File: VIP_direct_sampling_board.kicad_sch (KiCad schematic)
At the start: 32 parts, among them U1 ${SIM.PARAMS}, U10 LM4132xMF-1.8, U11 DC4759J5020AHF-1, U12 LAT-3, U2 TMUX1104DGSR, U7 MAR-8ASM+, U8 RBP-140+, U9 TSS-23ULN+, X1 B3715

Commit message: PWR progress
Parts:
- added C10: Cbypass, symbol Device:C
- added C8: C, symbol Device:C
- added C9: CBlock, symbol Device:C
- added L4: L, symbol Device:L
- added R10: Rbias, symbol Device:R_US
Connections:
- net GND: now also C10.2; no longer U7.3 (RF-OUT/DC-IN)
- net at U12.2 (OUT): now also C8.1; no longer U7.1 (RF-IN)
- new net: L4.2, R10.2
- new net: C9.1, L4.1, U7.3 (RF-OUT/DC-IN)
- new net: C8.2, U7.1 (RF-IN)
- new net 5V_SW: C10.1, R10.1
- new net RF_OUT: C9.2
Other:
- added sheet power (power.kicad_sch)
- note added: "3.7V"
- note added: "4:1 RF MUX"
- note added: "Bandpass Filter"
- note added: "RFFE First LNA"
- note added: "RFFE Monolithic Amplifier"
- note added: "SAW Filter"
- moved on the sheet: U7

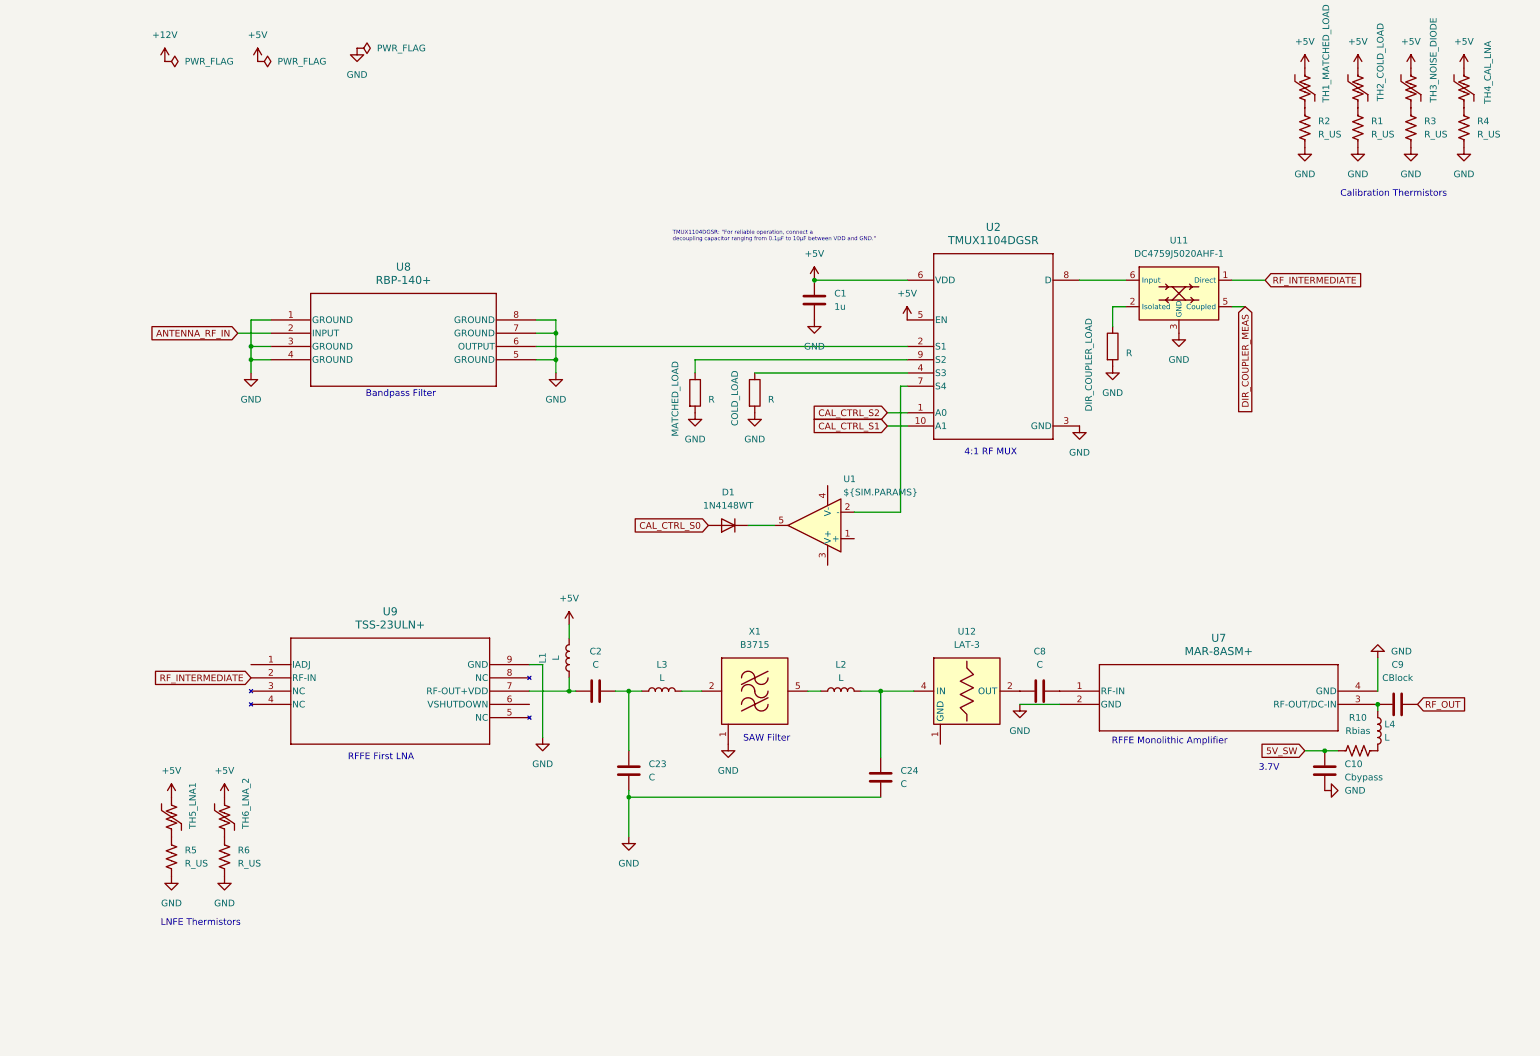
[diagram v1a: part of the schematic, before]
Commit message: PSA amplifiers
Replaced MAR amplifiers for PSA amplifiers which require much lower power but have similar gain
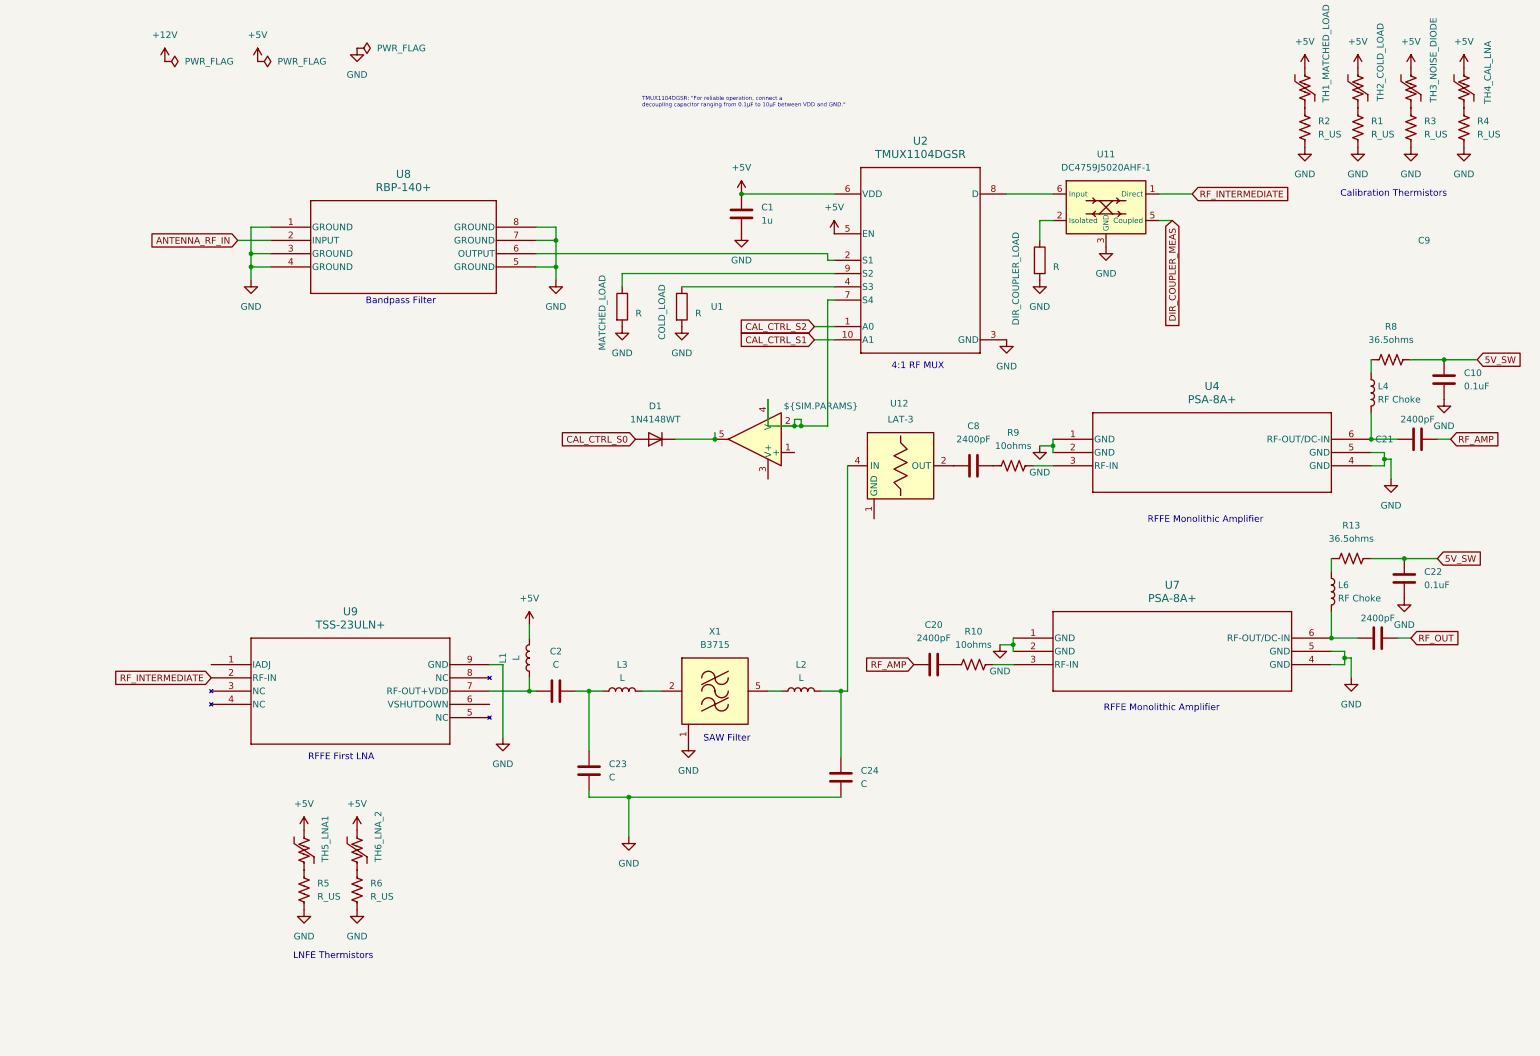
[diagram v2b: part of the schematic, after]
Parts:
- removed U7: MAR-8ASM+, WW107_MNC, symbol VIP_PocketQube_PCB_Library:MAR-8ASM+
- added C20, C21: 2400pF, symbol Device:C
- added C22: 0.1uF, symbol Device:C
- added L6: RF Choke, symbol Device:L
- added R13, R8: 36.5ohms, symbol Device:R_US
- added R9: 10ohms, symbol Device:R_US
- added U4, U7: PSA-8A+, CA1389_MNC, symbol 2026-10-19_10-28-32:PSA-8A+
- C10: value Cbypass -> 0.1uF
- C8: value C -> 2400pF
- C9: value CBlock -> 2400pF
- L4: value L -> RF Choke
- R10: value Rbias -> 10ohms
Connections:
- net 5V_SW: now also C22.1, R13.2, R8.2; no longer R10.1
- net GND: now also C22.2, U4.1 (GND), U4.2 (GND), U4.4 (GND), U4.5 (GND), U7.1 (GND), U7.2 (GND), U7.4 (GND), U7.5 (GND)
- net RF_OUT: now also C21.2; no longer C9.2
- net at R10.2: now also U7.3 (RF-IN); no longer L4.2
- net at C9.1: now also L4.2, U4.6 (RF-OUT/DC-IN); no longer L4.1
- net at C8.2: now also R9.1
- net at U1.2 (-), U2.7 (S4): now also U1.4 (V-)
- new net: C21.1, L6.2, U7.6 (RF-OUT/DC-IN)
- new net: R9.2, U4.3 (RF-IN)
- new net: C20.2, R10.1
- new net: L6.1, R13.1
- new net: L4.1, R8.1
- new net RF_AMP: C20.1, C9.2
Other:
- note removed: "3.7V"
- moved on the sheet: C1, C2, C23, C24, C8, C9, COLD_LOAD, D1, DIR_COUPLER_LOAD, L1, L2, L3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

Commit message: amps
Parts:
- removed U10: LM4132xMF-1.8, Package_TO_SOT_SMD:SOT-23-5, symbol Reference_Voltage:LM4132xMF-1.8
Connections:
- net +5V: no longer L1.2
- net 5V_SW renamed 5V_F
- new net 3V0_RF: L1.2
- now unconnected: U1.2 (-), U1.4 (V-), U2.7 (S4)

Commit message: Merging Branch to Main
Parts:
- removed C20, C21: 2400pF, symbol Device:C
- removed C22: 0.1uF, symbol Device:C
- removed C23, C24: C, symbol Device:C
- removed DIR_COUPLER_LOAD: R, symbol Device:R
- removed L6: RF Choke, symbol Device:L
- removed R10: 10ohms, symbol Device:R_US
- removed R13: 36.5ohms, symbol Device:R_US
- removed U1: ${SIM.PARAMS}, symbol Simulation_SPICE:OPAMP
- removed U12: LAT-3, RF_Mini-Circuits:Mini-Circuits_MMM168_LandPatternPL-225, symbol RF:LAT-3
- removed U4, U7: PSA-8A+, CA1389_MNC, symbol 2026-10-19_10-28-32:PSA-8A+
- added 50_OHM_LOAD: R, symbol Device:R
- added C11, C5: 0.1uF, symbol Device:C
- added C12, C4: 2400pF, symbol Device:C
- added C3: 36 pF, symbol Device:C
- added C30, C31, C32, C33, C34, C35, C39, C42, C43: 1uF, symbol Device:C
- added C36, C40, C41, C6, C7: 10uF, symbol Device:C
- added C37: 22uF, symbol Device:C
- added C38: 330pF, symbol Device:C
- added J1: Conn_01x06_Pin, symbol Connector:Conn_01x06_Pin
- added L7: 10uH, symbol Device:L
- added Q1: EMH3, Package_TO_SOT_SMD:SOT-563, symbol Transistor_BJT:EMH3
- added R11, R16: 10, symbol Device:R_US
- added R14: 5, symbol Device:R_US
- added R15, R17: 36.5, symbol Device:R_US
- added R18: 1, symbol Device:R_US
- added R19: 10k, symbol Device:R_US
- added R20: 100k, symbol Device:R_US
- added R21: 100ohms, symbol Device:R_US
- added R7: R_US, symbol Device:R_US
- added TH6_LNA_2: ~, symbol Device:Thermistor_US
- added U1, U6: JEBT-4R2GW+, BL301_MNC, symbol VIP_PocketQube_PCB_Library:JEBT-4R2GW+
- added U10, U7: PSA-8A+, CA1389_MNC, symbol VIP_PocketQube_PCB_Library:PSA-8A+
- added U12, U14, U22: LP5907MFX-3.0, Package_TO_SOT_SMD:SOT-23-5, symbol Regulator_Linear:LP5907MFX-3.0
- added U13: LM66100DCK, Package_TO_SOT_SMD:SOT-363_SC-70-6, symbol Power_Management:LM66100DCK
- added U21: TPS22918TDBVRQ1, DBV0006A_N, symbol TPS22918:TPS22918TDBVRQ1
- added U3: DAT-15R5-SP+, DG983-2_MNC, symbol VIP_PocketQube_PCB_Library:DAT-15R5-SP+
- added U4: ADS7830IPWT, PW16, symbol VIP_PocketQube_PCB_Library:ADS7830IPWT
- added U5: TSS-23ULN+, MC1631-1_MNC, symbol VIP_PocketQube_PCB_Library:TSS-23ULN+
- C10: value 0.1uF -> 2400pF
- C2: value C -> 36 pF
- C8: value 2400pF -> 0.1uF
- D1: value 1N4148WT -> GC6002-350A
- L2, L3: value L -> 68 nH
- L4: value RF Choke -> L
- R8: value 36.5ohms -> 2k
- R9: value 10ohms -> 2k
- renumbered COLD_LOAD to COLD_LOAD1, MATCHED_LOAD to MATCHED_LOAD1, TH1_MATCHED_LOAD to TH1_MATCHED_LOAD1, TH2_COLD_LOAD to TH2_COLD_LOAD1, TH3_NOISE_DIODE to TH3_NOISE_DIODE1, TH4_CAL_LNA to TH4_CAL_LNA1, TH5_LNA1 to TH5_LNA0, TH6_LNA_2 to TH6_LNA_1
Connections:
- net DIR_COUPLER_MEAS is gone; now on an unnamed net: U11.5 (Coupled)
- net +12V: now also J1.5 (Pin_5), R21.1
- net +5V: now also C31.1, J1.1 (Pin_1), TH6_LNA_2.1, U13.1 (VIN); no longer C1.1, U2.6 (VDD)
- net 3V0_RF: now also C1.1, U2.6 (VDD), U9.6 (VSHUTDOWN), C43.1, U1.24 (DC), U22.5 (OUT), U3.13 (VDD), U3.6 (VDD), U3.9 (VDD), U5.6 (VSHUTDOWN), U6.24 (DC); no longer L1.2
- net 5V_F: now also C32.1, C36.2, L7.2, R18.1, U14.1 (IN), U14.3 (EN), U21.1 (VIN); no longer C10.1, R8.2
- net CAL_CTRL_S0: now also Q1.2 (B1); no longer D1.2 (A)
- net GND: now also C2.2, C8.2, U2.7 (S4), 50_OHM_LOAD.2, C11.2, C3.2, C30.2, C31.2, C32.2, C33.2, C34.2, C35.2, C36.1, C37.2, C38.2, C39.2, C40.2, C41.2, C42.2, C43.2, C5.2, C6.2, C7.2, J1.2 (Pin_2), J1.6 (Pin_6), R20.2, R7.2, U1.1 (GROUND), U1.11 (GROUND), U1.12 (GROUND), U1.13 (GROUND), U1.14 (GROUND), U1.16 (GROUND), U1.17 (GROUND), U1.18 (GROUND), U1.19 (GROUND), U1.2 (GROUND), U1.20 (GROUND), U1.21 (GROUND), U1.22 (GROUND), U1.23 (GROUND), U1.3 (GROUND), U1.4 (GROUND), U1.5 (GROUND), U1.6 (GROUND), U1.7 (GROUND), U1.8 (GROUND), U1.9 (GROUND), U10.1 (GND), U10.2 (GND), U10.4 (GND), U10.5 (GND), U12.2 (GND), U13.2 (GND), U13.5 (ST), U14.2 (GND), U21.2 (GND), U22.2 (GND), U3.10 (GND), U3.11 (GND), U3.12 (GND), U3.15 (C8), U3.16 (C4), U3.17 (C2), U3.18 (GND), U3.19 (C1), U3.20 (C0.5), U3.21 (GND), U4.11 (COM), U4.12 (A0), U4.13 (A1), U4.8 (CH7), U4.9 (GND), U5.9 (GND), U6.1 (GROUND), U6.11 (GROUND), U6.12 (GROUND), U6.13 (GROUND), U6.14 (GROUND), U6.16 (GROUND), U6.17 (GROUND), U6.18 (GROUND), U6.19 (GROUND), U6.2 (GROUND), U6.20 (GROUND), U6.21 (GROUND), U6.22 (GROUND), U6.23 (GROUND), U6.3 (GROUND), U6.4 (GROUND), U6.5 (GROUND), U6.6 (GROUND), U6.7 (GROUND), U6.8 (GROUND), U6.9 (GROUND), U7.1 (GND), U7.2 (GND), U7.4 (GND), U7.5 (GND); no longer C10.2
- net RF_OUT: now also C12.2
- net at U2.4 (S3): now also U5.2 (RF-IN); no longer COLD_LOAD1.1
- net 5V_SW: now reaches C8.1
- net 5V_SW: now also C11.1, C30.1, C41.1, C42.1, R15.2, R17.2, U12.1 (IN), U21.5 (QOD), U21.6 (VOUT), U22.1 (IN), U22.3 (EN)
- net 3V0_TLM: now reaches R9.1
- net 3V0_TLM: now also R8.1, C34.1, C6.1, R14.2, U14.5 (OUT); no longer C8.2
- net at L2.2: now also X1.2 (IN)
- net CAL_NOISE_DIODE: now reaches R3.1, TH3_NOISE_DIODE1.2
- net CAL_NOISE_DIODE: now also U4.3 (CH2)
- net I2C_DSA_SCL: now reaches R9.2
- net I2C_DSA_SCL: now also U3.4 (CLOCK), U4.14 (SCL)
- net at L3.1: now also X1.5 (OUT); no longer C2.2
- net at L2.1: now also C2.1, U1.10 (RF/DC); no longer X1.5 (OUT)
- net at L3.2: now also C3.1, U3.2 (RFIN); no longer X1.2 (IN)
- net at C9.1: now also L1.1, U7.6 (RF-OUT/DC-IN); no longer L4.2
- net at U11.2 (Isolated): now also 50_OHM_LOAD.1
- net at L4.1: now also C12.1, U10.6 (RF-OUT/DC-IN); no longer R8.1
- net CAL_COLD_LOAD: now reaches R1.1, TH2_COLD_LOAD1.2
- net CAL_COLD_LOAD: now also U4.2 (CH1)
- net CAL_LNA: now reaches R4.1, TH4_CAL_LNA1.2
- net CAL_LNA: now also U4.4 (CH3)
- net CAL_MATCH_LOAD: now reaches R2.1, TH1_MATCHED_LOAD1.2
- net CAL_MATCH_LOAD: now also U4.1 (CH0)
- net RFCHAIN_LNA_0: now reaches R5.1, TH5_LNA0.2
- net RFCHAIN_LNA_0: now also U4.5 (CH4)
- net RFCHAIN_LNA_1: now reaches R6.1, TH6_LNA_1.2
- net RFCHAIN_LNA_1: now also U4.6 (CH5)
- net RF_AMP: no longer names the net of C9.2
- net RF_AMP: now also C10.1
- new net: U5.7 (RF-OUT+VDD), U6.15 (RF)
- new net: COLD_LOAD1.1, U6.10 (RF/DC)
- new net: D1.2 (A), Q1.1 (E1)
- new net: R16.2, U10.3 (RF-IN)
- new net: L4.2, R17.1
- new net: C37.1, R18.2
- new net: L1.2, R15.1
- new net: R11.2, U7.3 (RF-IN)
- new net: C7.1, R14.1, U4.16 (VDD+)
- new net: C5.1, U4.10 (REFIN/REFOUT)
- new net: R19.2, R20.1, U21.3 (ON)
- new net: C10.2, R16.1
- new net: C4.2, R11.1
- new net: U1.15 (RF), U9.7 (RF-OUT+VDD)
- new net: C38.1, U21.4 (CT)
- new net 12V_F: C39.1, C40.1, Q1.6 (C1), R21.2
- new net 3V0_COLD: C33.1, U12.5 (OUT)
- new net 5V_Diode: C35.1, U13.3 (~{CE}), U13.6 (VOUT)
- new net 5V_diode: L7.1
- new net COLD_LNA_EN: U12.3 (EN)
- new net DSA_LE: U3.5 (LE)
- new net DSA_SDA: U3.3 (DATA)
- new net DSA_TO_AMP: C4.1, U3.14 (RFOUT)
- new net I2C_SDA: R8.2, U4.15 (SDA)
- new net RFCHAIN_LNA_2: R7.1, TH6_LNA_2.2, U4.7 (CH6)
- new net RF_PWR_EN: R19.1
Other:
- removed sheet power
- note added: "3V LDO: Main LNA/digital RF. Switched by master switch (SYS-2)."
- note added: "Bias Tee"
- note added: "Calibration Circuit"
- note added: "Cold LNA, on only during cold calibration. Default OFF when enable is not asserted (PWR-6)"
- note added: "Current adjust pad. Must be left floating for nominal operation"
- note added: "Digital Step Attenuator"
- note added: "Diode - Reverse Current Blocking Circuit"
- note added: "LC low-pass for ripple spec"
- note added: "LDO for Telemetry"
- note added: "Master power switch for the RF hardware"
- note added: "MicroD"
- note added: "Monolithic Amplifier"
- note added: "Noise Diode"
- note added: "RF Amplifier-Filter Chain"
- note added: "Telemetry ADC"
- note added: "Temperature Monitoring"
- note added: "Voltage Step-Down & Power Control"
- note removed: "Bandpass Filter"
- note removed: "RFFE First LNA"
- note removed: "RFFE Monolithic Amplifier"
- moved on the sheet: C1, COLD_LOAD1, D1, MATCHED_LOAD1, R1, R2, R3, R4, R5, R6, TH1_MATCHED_LOAD1, TH2_COLD_LOAD1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
